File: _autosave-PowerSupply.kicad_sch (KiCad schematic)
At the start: 40 parts

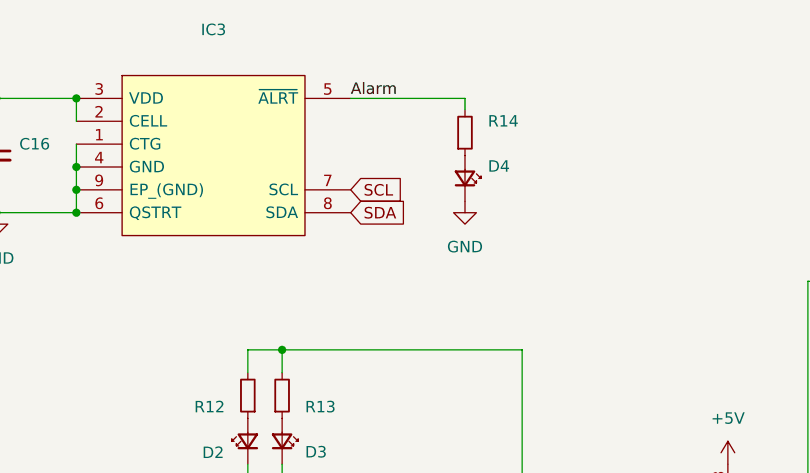
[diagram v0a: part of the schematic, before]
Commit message: layout for changed chematic
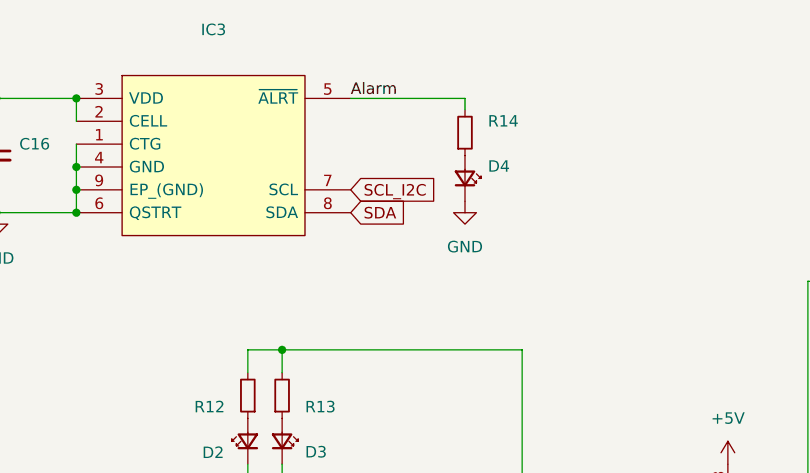
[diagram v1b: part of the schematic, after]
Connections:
- net SCL renamed SCL_I2C
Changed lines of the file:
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@@
     )
   )
-  (global_label "SCL" (shape input) (at 151.13 49.53 0) (fields_autoplaced)
+  (global_label "SCL_I2C" (shape input) (at 151.13 49.53 0) (fields_autoplaced)
     (effects (font (size 1.27 1.27)) (justify left))
-    (property "Intersheet References" "${INTERSHEET_REFS}" (id 0) (at 157.0507 49.4506 0)
+    (property "Intersheet References" "${INTERSHEET_REFS}" (id 0) (at 161.1026 49.4506 0)
       (effects (font (size 1.27 1.27)) (justify left) hide)
     )
